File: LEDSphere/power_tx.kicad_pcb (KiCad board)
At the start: 2 copper layers, 124 x 120 mm, 62 parts, among them J1 USB_C_Receptacle_USB2.0, M1 Motor_DC, Q1 D882, Q2 D882, Q3 BSS138, Q4 BSS138, Q5 BSS138, Q6 BSS138, Q7 BSS138, Q8 BSS138, SW1 SW_DIP_x03, U1 Pin-Connector, U10 HT7550-1-SOT89, U11 CH224K, U2 Pin-Connector, U3 Pin-Connector, U4 Pin-Connector, U5 Pin-Connector, U6 Pin-Connector, U7 4017, U8 TPS54302

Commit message: Starting Layout
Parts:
- removed the C1 at (134.2, 150.2)
- removed L3: 10µH, Inductor_SMD:L_Bourns_SRP7028A_7.3x6.6mm
- removed the Q1 at (115.2, 146.3)
- removed the Q2 at (122.7, 147.4)
- removed the R1 at (100.9, 135.1)
- removed the U1 at (102.3, 132.7)
- removed the U2 at (105.3, 132.5)
- removed the U3 at (134.3, 122.1)
- removed U5, U6: Pin-Connector, my_footprints:Pin_2mm
- added C11: 1nF, Capacitor_SMD:C_0603_1608Metric, F.Cu at (234.8, 71.3)
- added C13: 10nF, Capacitor_SMD:C_0603_1608Metric, F.Cu at (234.8, 73.8)
- added C15: 1uF, Capacitor_SMD:C_0402_1005Metric, F.Cu at (258.5, 78.6)
- added C18: 1uF, Capacitor_SMD:C_0805_2012Metric, F.Cu at (247.0, 80.2)
- added C19: 1uF, Capacitor_THT:C_Radial_D8.0mm_H7.0mm_P3.50mm, F.Cu at (145.1, 150.1)
- added C20: 1uF, Capacitor_SMD:C_0805_2012Metric, F.Cu at (247.0, 83.2)
- added C21: 1uF, Capacitor_SMD:C_0603_1608Metric, F.Cu at (234.8, 76.3)
- added C22: 10µ, 50V, Capacitor_SMD:C_1206_3216Metric, F.Cu at (180.9, 142.9)
- added C23: 220pF, Capacitor_SMD:C_0402_1005Metric, F.Cu at (258.5, 80.6)
- added C24: 220pF, Capacitor_SMD:C_0402_1005Metric, F.Cu at (258.5, 82.6)
- added C25: 100nF, Capacitor_SMD:C_0603_1608Metric, F.Cu at (234.8, 78.8)
- added C26: 0.1uF, Capacitor_SMD:C_0603_1608Metric, F.Cu at (234.8, 81.3)
- added C27: 100nF, Capacitor_SMD:C_0603_1608Metric, F.Cu at (238.8, 68.8)
- added C28: 50nF, Capacitor_SMD:C_0603_1608Metric, F.Cu at (238.8, 71.3)
- added C30: 1uF, Capacitor_SMD:C_0805_2012Metric, F.Cu at (247.0, 86.2)
- added C31: 1uF, Capacitor_SMD:C_0805_2012Metric, F.Cu at (247.0, 89.2)
- added C4: 10µF, Capacitor_SMD:C_0805_2012Metric, F.Cu at (247.0, 77.2)
- added C5: 1µF, Capacitor_SMD:C_0603_1608Metric, F.Cu at (85.6, 92.5)
- added D1: LED, LED_SMD:LED_0805_2012Metric, F.Cu at (82.8, 93.1)
- added D3: D, Diode_SMD:D_SMA, F.Cu at (250.0, 102.1)
- added Q7: Si2319CDS, Package_TO_SOT_SMD:SOT-23, F.Cu at (186.5, 148.0)
- added Q8: Si2319CDS, Package_TO_SOT_SMD:SOT-23, F.Cu at (193.6, 150.7)
- added R11: 1k, Resistor_SMD:R_0603_1608Metric, F.Cu at (82.6, 91.4)
- added R19: 100k, Resistor_SMD:R_0402_1005Metric, F.Cu at (250.7, 84.6)
- added R23: 1k, Resistor_SMD:R_0402_1005Metric, F.Cu at (250.7, 86.6)
- added R24: 10k, Resistor_SMD:R_0402_1005Metric, F.Cu at (250.7, 88.6)
- added R25: 22R, Resistor_SMD:R_0402_1005Metric, F.Cu at (250.7, 90.6)
- added R27: 51R, Resistor_SMD:R_0603_1608Metric, F.Cu at (238.8, 76.3)
- added R28: 51R, Resistor_SMD:R_0603_1608Metric, F.Cu at (238.8, 78.8)
- added R29: 5R, Resistor_SMD:R_0603_1608Metric, F.Cu at (238.8, 81.3)
- added R30: 2.2R, Resistor_SMD:R_0603_1608Metric, F.Cu at (242.8, 68.8)
- added R31: 10k, Resistor_SMD:R_0603_1608Metric, F.Cu at (242.8, 71.3)
- added R32: 10k, Resistor_SMD:R_0603_1608Metric, F.Cu at (242.8, 73.8)
- added R33: 5R, Resistor_SMD:R_0603_1608Metric, F.Cu at (242.8, 76.3)
- added R34: 5R, Resistor_SMD:R_0603_1608Metric, F.Cu at (242.8, 78.8)
- added R4: 5.1k, Resistor_SMD:R_0402_1005Metric, F.Cu at (84.5, 99.3)
- added R5: 5.1k, Resistor_SMD:R_0402_1005Metric, F.Cu at (83.4, 99.3)
- added R7: 1k, Resistor_SMD:R_0402_1005Metric, F.Cu at (85.0, 90.5)
- added R9: 47k, Resistor_SMD:R_0402_1005Metric, F.Cu at (85.5, 99.3)
- added RV1: FRQ_ADJ (20K), Footprints:TRIM_3362P-1-203LF, F.Cu at (203.2, 155.6)
- added U8: UCC27714DR, Footprints:D0014A, F.Cu at (247.4, 112.8)
- C16: value 100nF -> 1uF; footprint Capacitor_SMD:C_0603_1608Metric -> Capacitor_SMD:C_0805_2012Metric
- C2: value 10µ, 50V -> 100nF; footprint Capacitor_SMD:C_1206_3216Metric -> Capacitor_SMD:C_0402_1005Metric
- D2: renamed from D1; footprint my_footprints:DIOM7959X265N -> Footprints:DIOM7959X262N
- J1: footprint my_footprints:USB_C_Receptacle -> Connector_USB:USB_C_Receptacle_GCT_USB4105-xx-A_16P_TopMnt_Horizontal
- L1: value 330µH -> 10µH; footprint Inductor_SMD:L_SXN_SMDRI127 -> Inductor_SMD:L_Bourns_SRP7028A_7.3x6.6mm
- M1: footprint my_footprints:motor -> Footprints:motor
- SW1: value SW_DIP_x03 -> ~; footprint Button_Switch_SMD:SW_DIP_SPSTx03_Slide_9.78x9.8mm_W8.61mm_P2.54mm -> Footprints:XKB5858-X-F-75
- SW2: footprint my_footprints:XKB5858-X-F-75 -> Footprints:XKB5858-X-F-75
- U1: renamed from U7; footprint Package_SO:SOP-16_3.9x9.9mm_P1.27mm -> Package_SO:STC_SOP-16_3.9x9.9mm_P1.27mm
- U2: renamed from U11; value CH224K -> CH221K; footprint Package_SO:SSOP-10-1EP_3.9x4.9mm_P1mm_EP2.1x3.3mm -> Package_TO_SOT_SMD:SOT-23-6
- U4: value Pin-Connector -> SG3525; footprint my_footprints:Pin_2mm -> Footprints:SO-16N_STM
- moved C2 170.6 mm to (258.5, 76.7), turned to 0 degrees
- moved L1 94.1 mm to (191.1, 98.0), turned to 90 degrees
- moved SW1 71.1 mm to (141.2, 42.2), turned to 0 degrees
- moved U4 33.2 mm to (101.5, 138.4), turned to 50 degrees
- moved SW2 1.56 mm to (129.5, 43.0)
- moved U2 0.73 mm to (84.4, 96.2)
- turned C8 to -84.699 degrees
- renumbered C3 to C1, C15 to C10, C7 to C12, C6 to C14, C9 to C17, C8 to C3, C4 to C6, C5 to C7, C13 to C8, C17 to C9, Q8 to Q1, Q3 to Q2, Q4 to Q3, Q5 to Q4, Q6 to Q5, Q7 to Q6, R4 to R1, R7 to R10, R13 to R12, R9 to R13, R16 to R14, R17 to R15, R2 to R16, R15 to R17, R3 to R18, R5 to R2, R25 to R20, R19 to R21, R18 to R22, R20 to R26, R8 to R3, R24 to R6, R14 to R8, R6 to R8, U8 to U3
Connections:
- C1 pad 1: Net-(U7-CLK) -> Net-(U1-CLK)
- C10 pad 1: Net-(U8-FB) -> Net-(U3-FB)
- C10 pad 2: Net-(C15-Pad2) -> Net-(C10-Pad2)
- C16 pad 1: +5V -> +12V
- C2 pad 1: VBUS -> GND
- C2 pad 2: GND -> +12V
- C6 pad 1: VBUS -> +12V
- C7 pad 1: VBUS -> +12V
- C8 pad 2: Net-(U8-SW) -> Net-(U3-SW)
- C9 pad 1: Net-(U8-FB) -> Net-(U3-FB)
- C9 pad 2: Net-(C15-Pad2) -> Net-(C10-Pad2)
- J1 pad A4: VBUS -> +12V
- J1 pad A9: VBUS -> +12V
- J1 pad B4: VBUS -> +12V
- J1 pad B9: VBUS -> +12V
- L1 pad 1: VBUS -> Net-(U3-SW)
- L1 pad 2: Net-(Q1-C) -> Motor
- Q1 pad 3: Net-(Q8-D) -> Net-(Q1-D)
- R1 pad 1: +5V -> +12V
- R1 pad 2: Net-(R4-Pad2) -> Net-(R1-Pad2)
- R12 pad 1: Net-(U8-FB) -> Net-(U3-FB)
- R14 pad 1: Net-(U8-FB) -> Net-(U3-FB)
- R15 pad 1: Net-(U8-FB) -> Net-(U3-FB)
- R16 pad 1: Net-(U8-FB) -> Net-(U3-FB)
- R18 pad 1: Net-(U8-FB) -> Net-(U3-FB)
- R2 pad 1: Net-(U7-CLK) -> Net-(U1-CLK)
- R21 pad 2: Net-(C15-Pad2) -> Net-(C10-Pad2)
- R8 pad 1: Net-(U8-FB) -> +12V
- R8 pad 2: Net-(C15-Pad2) -> Net-(Q1-D)
- SW1 pad 1: Net-(U11-CFG1) -> unconnected-(SW1-Pad1)
- SW1 pad 2: Net-(U11-CFG2) -> Net-(U1-CLK)
- SW1 pad 3: Net-(U11-CFG3) -> unconnected-(SW1-Pad3)
- SW1 pad 4: GND -> Net-(R1-Pad2)
- SW1 pad 5: GND -> Net-(U1-CLK)
- SW1 pad 6: GND -> Net-(R1-Pad2)
- SW2 pad 4: +5V -> +12V
- SW2 pad 6: +5V -> +12V
- U1 pad 14: Net-(U7-CLK) -> Net-(U1-CLK)
- U1 pad 16: +5V -> +12V
- U2 pad 1: VDD -> Net-(U2-VDD)
- U2 pad 2: Net-(U11-CFG2) -> GND
- U2 pad 3: Net-(U11-CFG3) -> Net-(D1-K)
- U2 pad 4: DP -> CC1
- U2 pad 5: DM -> CC2
- U2 pad 6: CC2 -> Net-(U2-CFG)
- U3 pad 2: Net-(U8-SW) -> Net-(U3-SW)
- U3 pad 3: VBUS -> +12V
- U3 pad 4: Net-(U8-FB) -> Net-(U3-FB)
- U3 pad 5: Net-(Q8-D) -> Net-(Q1-D)
- U4 pad 1: Net-(Q1-C) -> GND
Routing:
- net Net-(U2-VDD): track 0.00 -> 3.42 mm
- net GND: track 0.00 -> 3.06 mm, vias 0 -> 1
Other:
- board text added: "12V IN"
- board text removed: "ON = 0, OFF = 1 1 0 0 5V 0 0 0 9V 0 0 1 12V 0 1 1 15V 0 1 0 20V"
- board text removed: "RS64c_PS"

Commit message: Start Layout
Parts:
- removed U10: HT7550-1-SOT89, Package_TO_SOT_SMD:SOT-89-3
- moved C15 160.1 mm to (113.8, 147.1), turned to -40 degrees
- moved R23 159.4 mm to (101.0, 141.4), turned to -130 degrees
- moved R25 149.4 mm to (112.8, 148.1), turned to 140 degrees
- moved R24 146.8 mm to (115.5, 145.9), turned to -40 degrees
- moved C11 145.2 mm to (112.3, 149.4), turned to -40 degrees
- moved C13 137.9 mm to (116.8, 145.2), turned to 140 degrees
- moved RV1 105.7 mm to (99.2, 136.5), turned to 140 degrees
- moved U8 11.6 mm to (241.1, 122.5)
- moved U4 7.65 mm to (108.1, 142.4)
- moved R4 0.52 mm to (85.0, 99.3)
- moved R9 0.52 mm to (86.0, 99.3)
- moved R7 0.39 mm to (85.0, 90.1)
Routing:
- net +12V: track 0.00 -> 31.8 mm
- net Net-(U4-NI): track 0.00 -> 20.1 mm
- net /PWM_LO: track 0.00 -> 14.5 mm
- net GND: track 3.06 -> 17.1 mm, vias 1 -> 4
- net Net-(U4-RT): track 0.00 -> 11.3 mm
- net /PWM_HI: track 0.00 -> 10.2 mm
- net Net-(U4-CT): track 0.00 -> 10.2 mm
- net CC2: track 0.00 -> 9.97 mm
- net Net-(R23-Pad2): track 0.00 -> 8.38 mm
- net Net-(U2-VDD): track 3.42 -> 11.4 mm
- net Net-(U4-DISCH): track 0.00 -> 7.86 mm
- net CC1: track 0.00 -> 6.35 mm
- net Net-(U4-SD): track 0.00 -> 5.39 mm
- net Net-(U4-SS): track 0.00 -> 3.75 mm
- net Net-(U4-COMP): track 0.00 -> 3.73 mm
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
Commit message: Initial Layout (Rounded Tracks)
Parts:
- removed the C12 at (120.8, 43.6)
- removed the R8 at (175.5, 57.5)
- removed U12, U13, U9: ~, my_footprints:JLC_tooling_hole
- C19: footprint Capacitor_THT:C_Radial_D8.0mm_H7.0mm_P3.50mm -> Capacitor_SMD:C_1206_3216Metric
- L2: renamed from REF**; value power_coil -> 8.1uH; footprint PCB Coils:power_coil -> Footprints:power_coil
- moved C2 175.5 mm to (84.9, 102.3), turned to 90 degrees
- moved C4 165.7 mm to (83.4, 103.0), turned to -90 degrees
- moved C24 155.6 mm to (119.2, 151.8), turned to -130 degrees
- moved C23 154.9 mm to (120.5, 151.0), turned to -40 degrees
- moved C18 152.3 mm to (104.8, 134.7), turned to -40 degrees
- moved R27 141.9 mm to (117.8, 150.3), turned to -40 degrees
- moved R28 139.1 mm to (118.8, 149.2), turned to -40 degrees
- moved R30 135.3 mm to (136.1, 152.0), turned to 180 degrees
- moved R34 131.2 mm to (136.0, 155.1)
- moved C31 128.1 mm to (132.0, 145.5)
- moved C20 125.5 mm to (142.9, 153.2)
- moved C30 123.8 mm to (139.4, 147.4)
- moved C21 123.3 mm to (139.1, 154.0)
- moved R32 120.6 mm to (150.0, 150.9), turned to -90 degrees
- moved C25 120.4 mm to (136.6, 148.4), turned to 90 degrees
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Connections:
- C3 pad 1: +5V -> +12V
- D2 pad A: (no net) -> GND
- D2 pad C: (no net) -> Motor
- L2 pad 1: (no net) -> Net-(C26-Pad2)
- L2 pad 2: (no net) -> GND
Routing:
- net +12V: track 31.8 -> 331.4 mm, vias 0 -> 2
- net GND: track 17.1 -> 136.2 mm, vias 4 -> 43
- net Net-(U3-FB): track 0.00 -> 58.9 mm, vias 0 -> 6
- net U4: track 0.00 -> 52.3 mm, vias 0 -> 2
- net U5: track 0.00 -> 47.6 mm
- net Net-(U1-Reset): track 0.00 -> 42.9 mm, vias 0 -> 2
- net /HS: track 0.00 -> 42.8 mm, vias 0 -> 3
- net U1: track 0.00 -> 40.7 mm, vias 0 -> 2
- net Motor: track 0.00 -> 39.0 mm
- net Net-(Q1-D): track 0.00 -> 37.6 mm, vias 0 -> 2
- net Disable: track 0.00 -> 28.9 mm, vias 0 -> 2
- net Net-(U1-CLK): track 0.00 -> 28.2 mm
- net Net-(U8-HO): track 0.00 -> 26.1 mm, vias 0 -> 2
- net /FET_LO: track 0.00 -> 21.0 mm
- net Net-(D3-K): track 0.00 -> 20.7 mm
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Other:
- board text removed: "27 Turns"
- board text removed: "~ 27 Mils"

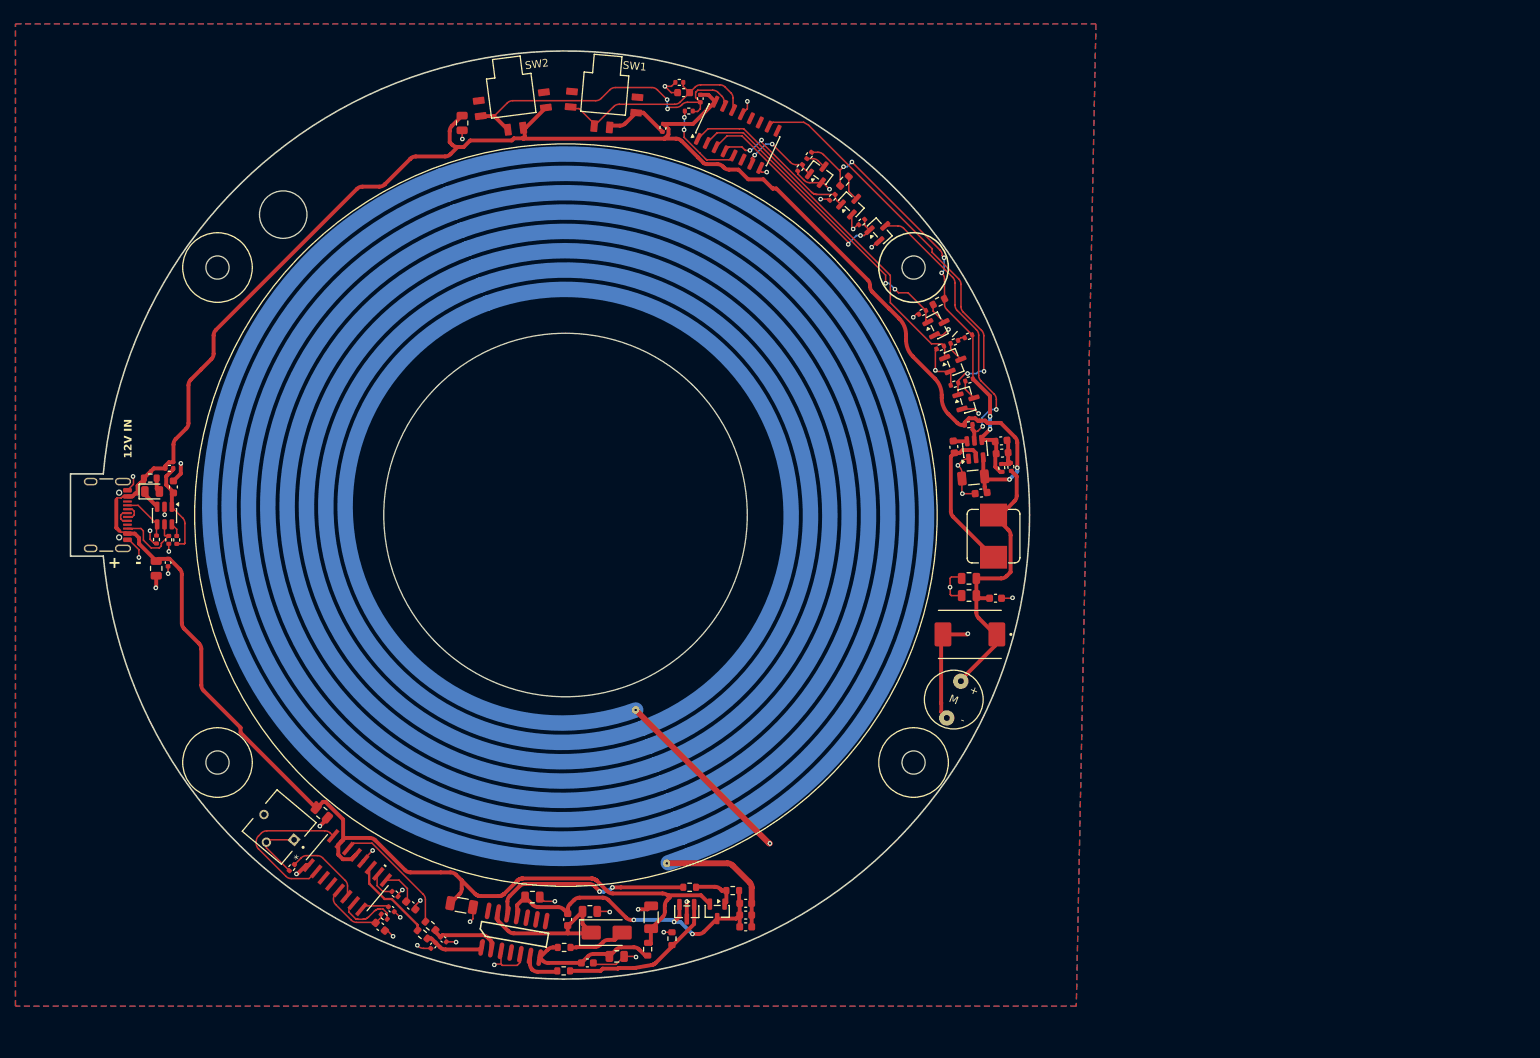
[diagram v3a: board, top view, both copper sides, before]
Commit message: Excluded Ground Pour
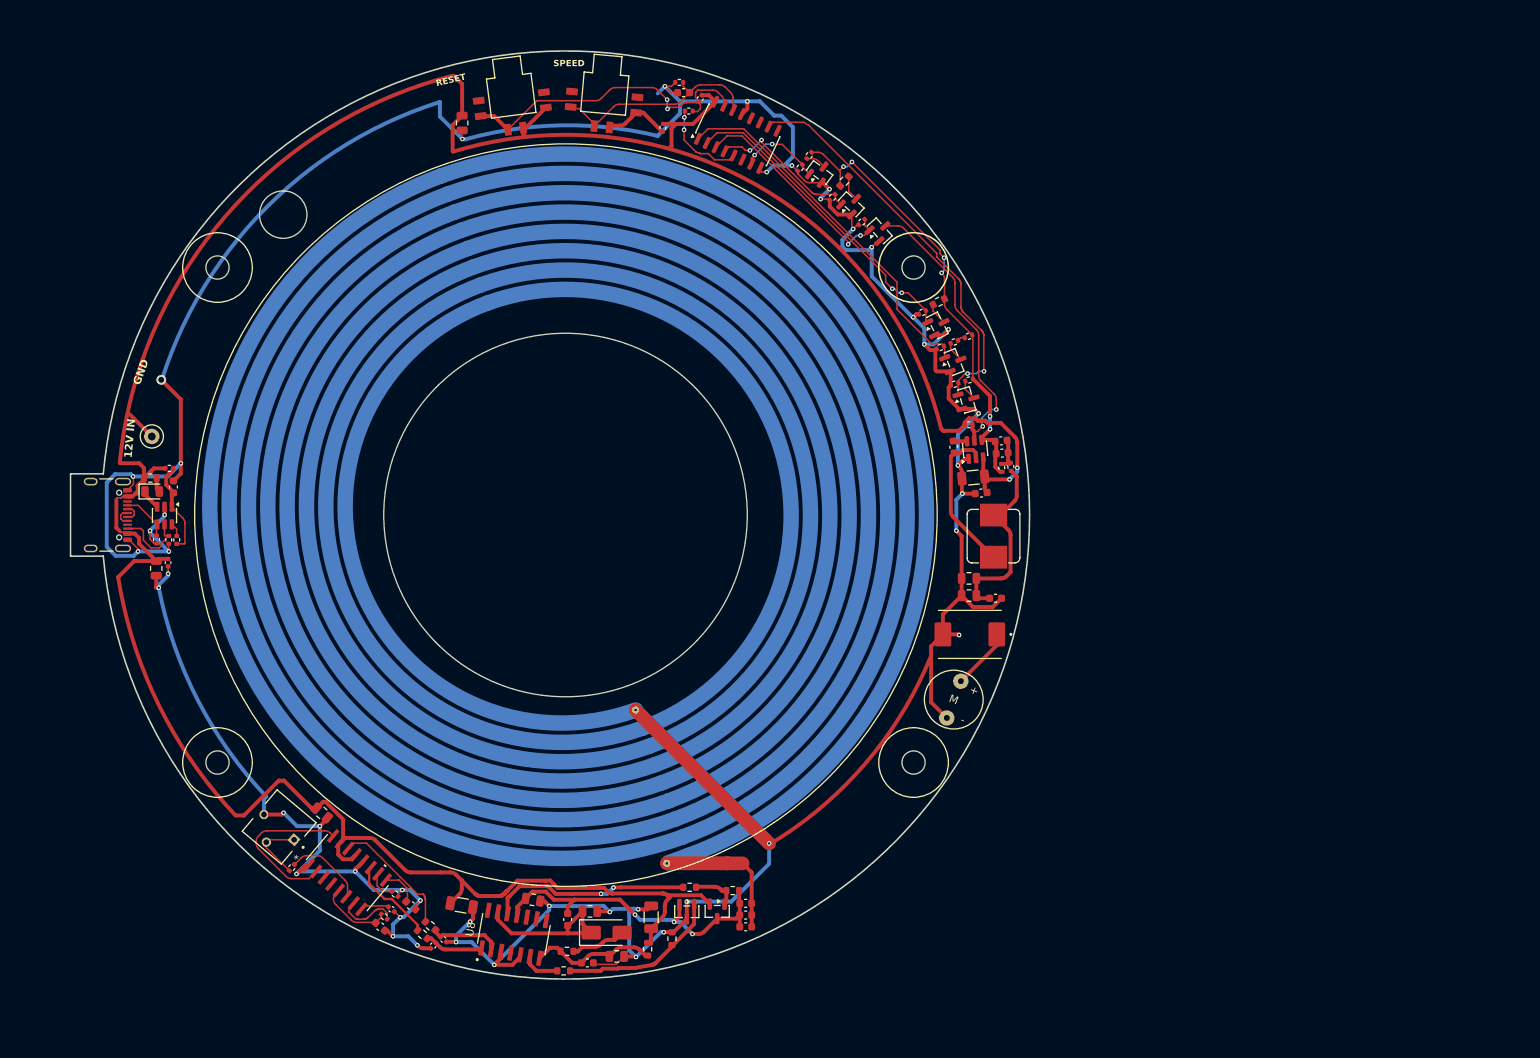
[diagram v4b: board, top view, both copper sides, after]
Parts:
- added TP1: TestPoint, TestPoint:TestPoint_Loop_D1.80mm_Drill1.0mm_Beaded, F.Cu at (82.8, 86.0)
- C28: value 50nF -> 68nF
- R11: value 1k -> 10k
- U8: footprint Footprints:D0014A -> Footprints:SOIC127P600X175-14N
- moved R30 0.62 mm to (136.5, 152.5)
- moved C31 0.35 mm to (132.1, 145.9), turned to -10 degrees
- turned C3 to -115 degrees
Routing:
- net GND: track 136.2 -> 398.1 mm, vias 43 -> 45
- net +12V: track 331.4 -> 181.7 mm
- net Motor: track 39.0 -> 32.8 mm
- net Net-(U8-VDD): track 18.9 -> 17.0 mm
- net Net-(C26-Pad2): track 17.5 -> 18.5 mm
- net Net-(U1-Reset): track 42.9 -> 42.0 mm
- net Net-(U8-HI): track 8.34 -> 7.63 mm
- net /HS: track 42.8 -> 43.3 mm
- removed copper zone on B.Cu, net GND
- removed copper zone on F.Cu, net GND
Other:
- board text added: "GND"
- board text added: "RESET"
- board text added: "SPEED"
- board text removed: "+"
- board text removed: "-"

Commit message: Modify RX Schm. + Adjusted TX Coil
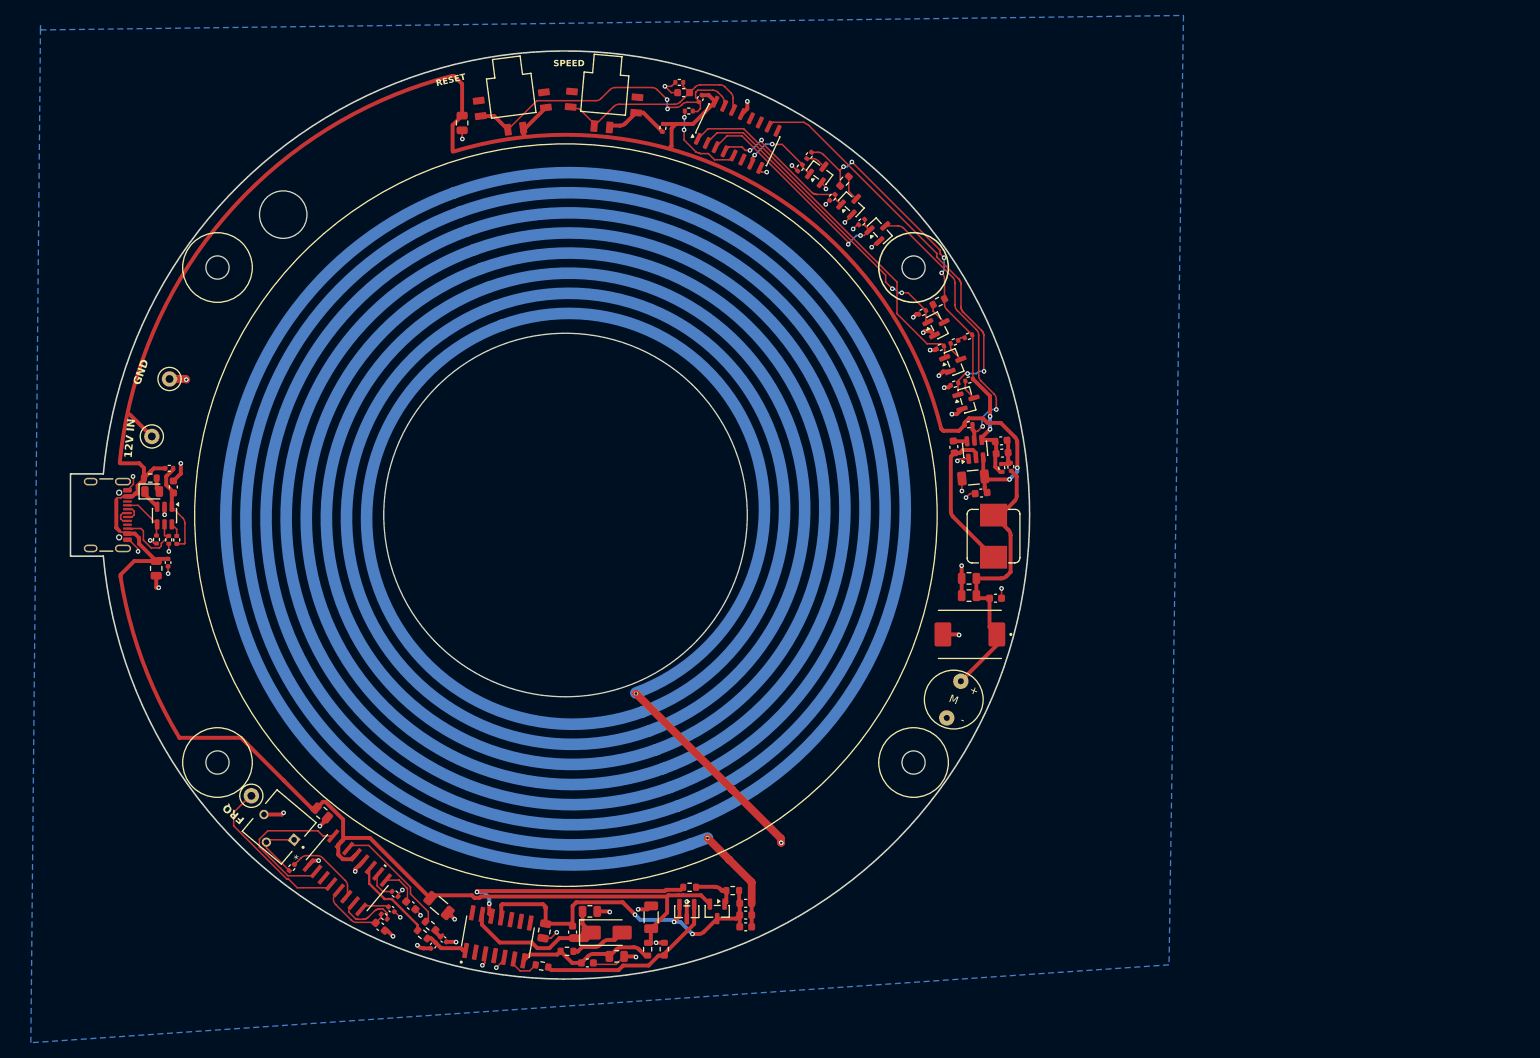
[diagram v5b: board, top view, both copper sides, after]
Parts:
- added TP2: TestPoint, TestPoint:TestPoint_Loop_D1.80mm_Drill1.0mm_Beaded, F.Cu at (85.1, 78.5)
- added TP3: TestPoint, TestPoint:TestPoint_Loop_D1.80mm_Drill1.0mm_Beaded, F.Cu at (95.7, 132.4)
- L2: value 8.1uH -> 8.1 uH
- moved C31 4.30 mm to (133.5, 149.9), turned to -100 degrees
- moved C19 2.94 mm to (119.9, 146.6), turned to -40 degrees
- moved R34 2.88 mm to (133.2, 154.4), turned to -10 degrees
- moved U8 2.09 mm to (127.5, 150.7)
- moved C25 1.74 mm to (137.2, 150.1)
- moved R32 1.69 mm to (149.0, 152.3)
- moved L2 0.99 mm to (136.7, 95.4)
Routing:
- net GND: track 398.1 -> 113.3 mm, vias 45 -> 51
- net /OSC: track 0.00 -> 21.0 mm
- net Net-(U8-LI): track 9.55 -> 1.88 mm
- net Net-(U8-HO): track 26.3 -> 31.4 mm
- net Motor: track 32.8 -> 37.8 mm
- net Net-(C26-Pad2): track 18.5 -> 13.8 mm
- net /HS: track 43.3 -> 47.7 mm
- net /FET_LO: track 21.0 -> 24.3 mm
- net +12V: track 181.7 -> 184.6 mm
- net Net-(U8-HI): track 7.63 -> 5.59 mm
- net Net-(U8-VDD): track 17.0 -> 18.6 mm
- net Net-(D3-K): track 20.7 -> 21.9 mm
- net Net-(U4-NI): track 21.3 -> 20.4 mm
- net Net-(U8-LO): track 5.06 -> 4.19 mm
- added copper zone on B.Cu, net GND
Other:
- board text added: "FRQ"
